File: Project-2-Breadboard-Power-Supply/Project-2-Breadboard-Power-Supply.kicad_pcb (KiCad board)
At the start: 2 copper layers, 35.1 x 53.3 mm, 17 parts, among them J1 Conn_01x02_Pin, J2 Conn_01x02_Pin, J3 Conn_01x03_Pin, J4 Conn_01x03_Pin, J5 Screw_Terminal_01x02, J6 Barrel_Jack_Switch, J7 Screw_Terminal_01x02, U1 LM7805_TO220, U2 LM317_TO-220

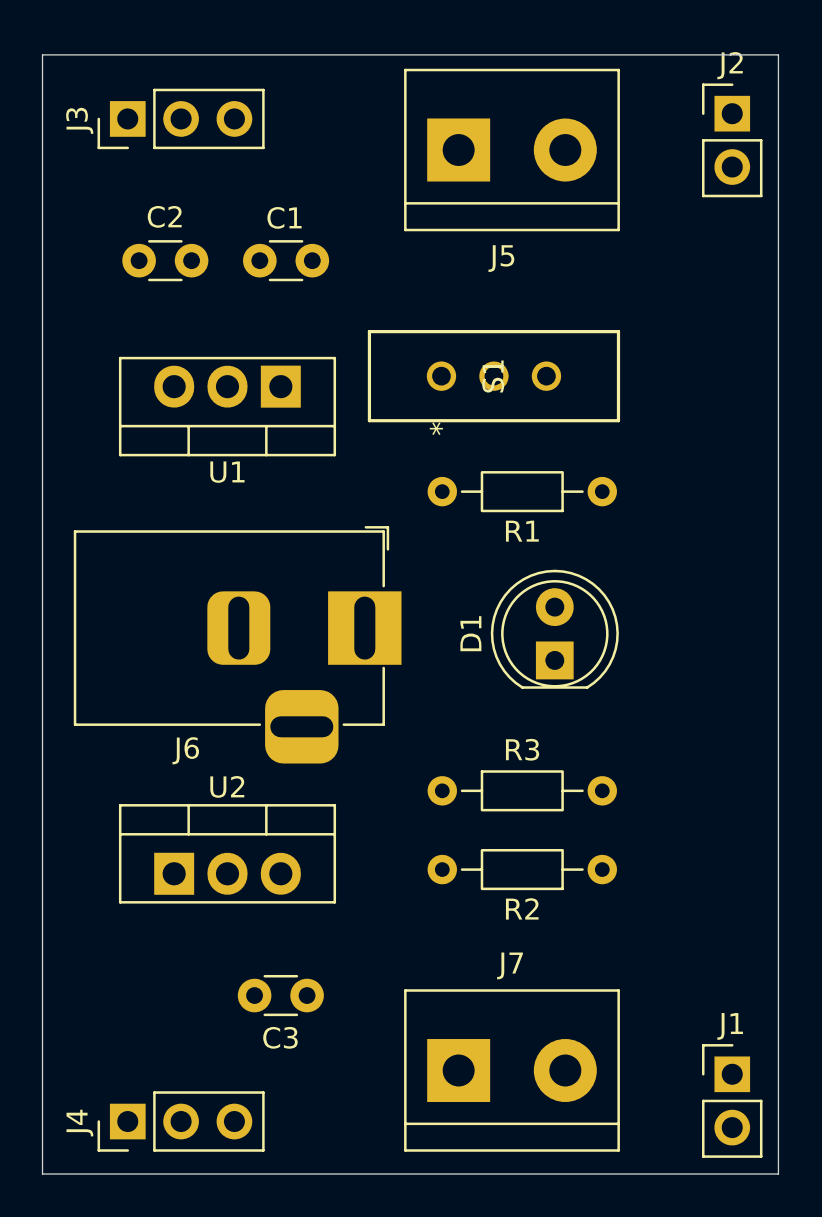
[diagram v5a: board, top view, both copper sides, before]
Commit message: update footprints' placement, and PCB's edge cuts
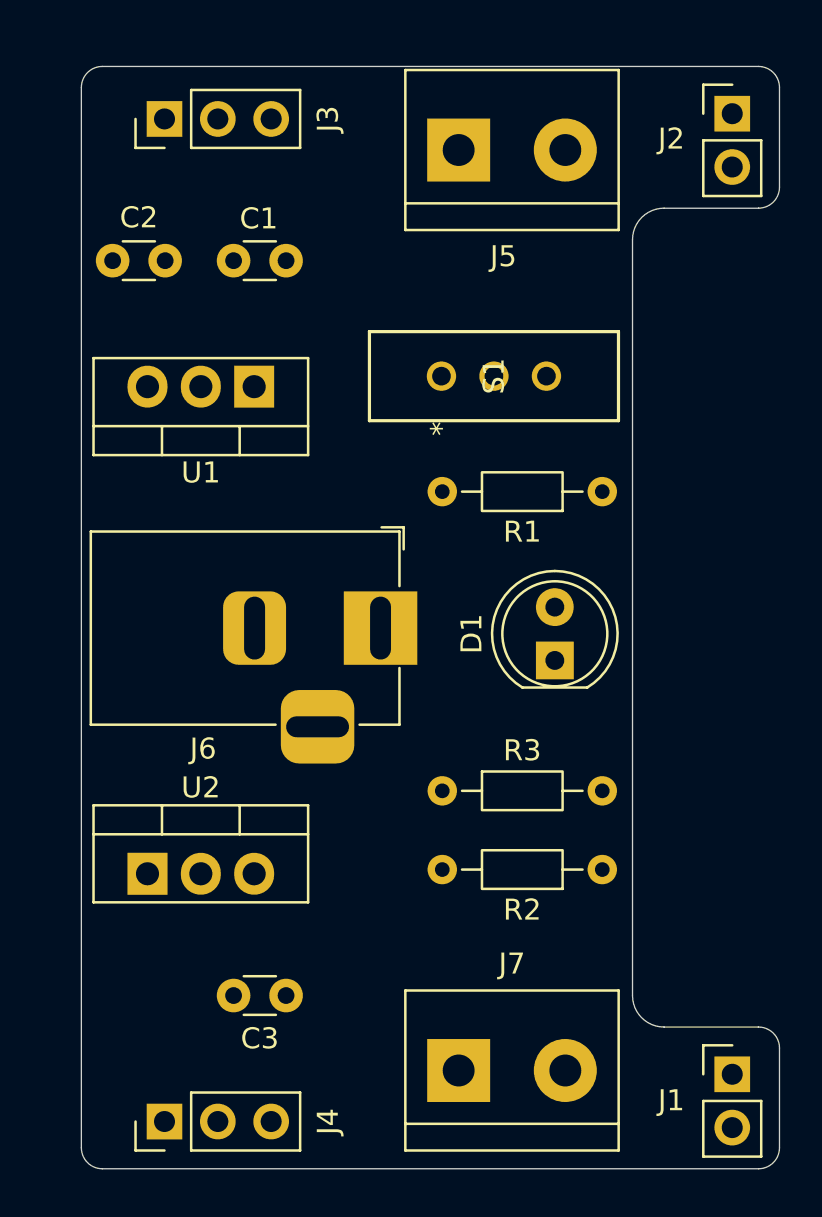
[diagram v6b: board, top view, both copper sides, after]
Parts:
- moved J3 1.75 mm to (34.0, 47.8)
- moved J4 1.75 mm to (34.0, 95.5)
- moved U1 1.27 mm to (38.2, 60.5)
- moved U2 1.27 mm to (33.1, 83.7)
- moved C2 1.26 mm to (31.5, 54.5)
- moved C1 1.25 mm to (39.8, 54.5)
- moved C3 1.00 mm to (39.8, 89.5)
- moved J6 0.75 mm to (44.2, 72.0)
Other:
- board size 35.1 x 53.3 mm -> 33.2 x 52.5 mm
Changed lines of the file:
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@@
 	(footprint "Connector_PinHeader_2.54mm:PinHeader_1x03_P2.54mm_Vertical"
 		(layer "F.Cu")
-		(at 32.21 95.5 90)
+		(at 33.96 95.5 90)
 		(descr "Through hole straight pin header, 1x03, 2.54mm pitch, single row")
 		(tags "Through hole pin header THT 1x03 2.54mm single row")
 		(property "Reference" "J4"
-			(at 0 -2.38 90)
+			(at 0 7.79 90)
 			(layer "F.SilkS")
 			(effects
@@
 	(footprint "Capacitor_THT:C_Disc_D3.0mm_W1.6mm_P2.50mm"
 		(layer "F.Cu")
-		(at 32.75 54.5)
+		(at 31.49 54.5)
 		(descr "C, Disc series, Radial, pin pitch=2.50mm, diameter*width=3.0*1.6mm^2, Capacitor, http://www.vishay.com/docs/45233/krseries.pdf")
 		(tags "C Disc series Radial pin pitch 2.50mm diameter 3.0mm width 1.6mm Capacitor")
@@
 	(footprint "Connector_PinHeader_2.54mm:PinHeader_1x03_P2.54mm_Vertical"
 		(layer "F.Cu")
-		(at 32.21 47.75 90)
+		(at 33.96 47.75 90)
 		(descr "Through hole straight pin header, 1x03, 2.54mm pitch, single row")
 		(tags "Through hole pin header THT 1x03 2.54mm single row")
 		(property "Reference" "J3"
-			(at 0 -2.38 90)
+			(at 0 7.79 90)
 			(layer "F.SilkS")
 			(effects
@@
 		(tags "Through hole pin header THT 1x02 2.54mm single row")
 		(property "Reference" "J2"
-			(at 0 -2.38 0)
+			(at -2.9 1.2 0)
 			(layer "F.SilkS")
 			(effects
@@
 	(footprint "Capacitor_THT:C_Disc_D3.0mm_W1.6mm_P2.50mm"
 		(layer "F.Cu")
-		(at 40.75 89.5 180)
+		(at 39.75 89.5 180)
 		(descr "C, Disc series, Radial, pin pitch=2.50mm, diameter*width=3.0*1.6mm^2, Capacitor, http://www.vishay.com/docs/45233/krseries.pdf")
 		(tags "C Disc series Radial pin pitch 2.50mm diameter 3.0mm width 1.6mm Capacitor")
@@
 	(footprint "Package_TO_SOT_THT:TO-220-3_Vertical"
 		(layer "F.Cu")
-		(at 34.42 83.7)
+		(at 33.15 83.7)
 		(descr "TO-220-3, Vertical, RM 2.54mm, see https://www.vishay.com/docs/66542/to-220-1.pdf")
 		(tags "TO-220-3 Vertical RM 2.54mm")
@@
 		(tags "Through hole pin header THT 1x02 2.54mm single row")
 		(property "Reference" "J1"
-			(at 0 -2.38 0)
+			(at -2.9 1.25 0)
 			(layer "F.SilkS")
 			(effects
@@
 	(footprint "Connector_BarrelJack:BarrelJack_Horizontal"
 		(layer "F.Cu")
-		(at 43.5 72)
+		(at 44.25 72)
 		(descr "DC Barrel Jack")
 		(tags "Power Jack")
@@
 	(footprint "Capacitor_THT:C_Disc_D3.0mm_W1.6mm_P2.50mm"
 		(layer "F.Cu")
-		(at 41 54.5 180)
+		(at 39.75 54.5 180)
 		(descr "C, Disc series, Radial, pin pitch=2.50mm, diameter*width=3.0*1.6mm^2, Capacitor, http://www.vishay.com/docs/45233/krseries.pdf")
 		(tags "C Disc series Radial pin pitch 2.50mm diameter 3.0mm width 1.6mm Capacitor")
@@
 	(footprint "Package_TO_SOT_THT:TO-220-3_Vertical"
 		(layer "F.Cu")
-		(at 39.5 60.5 180)
+		(at 38.23 60.5 180)
 		(descr "TO-220-3, Vertical, RM 2.54mm, see https://www.vishay.com/docs/66542/to-220-1.pdf")
 		(tags "TO-220-3 Vertical RM 2.54mm")
@@
 		)
 	)
-	(gr_rect
-		(start 28.15 44.7)
-		(end 63.2 98)
+	(gr_arc
+		(start 30 46.25)
+		(mid 30.292893 45.542893)
+		(end 31 45.25)
+		(stroke
+			(width 0.05)
+			(type default)
+		)
+		(layer "Edge.Cuts")
+	)
+	(gr_line
+		(start 30 96.75)
+		(end 30 46.25)
+		(stroke
+			(width 0.05)
+			(type default)
+		)
+		(layer "Edge.Cuts")
+	)
+	(gr_arc
+		(start 31 97.75)
+		(mid 30.292893 97.457107)
+		(end 30 96.75)
+		(stroke
+			(width 0.05)
+			(type default)
+		)
+		(layer "Edge.Cuts")
+	)
+	(gr_line
+		(start 56.25 53.5)
+		(end 56.25 89.5)
+		(stroke
+			(width 0.05)
+			(type default)
+		)
+		(layer "Edge.Cuts")
+	)
+	(gr_arc
+		(start 56.25 53.5)
+		(mid 56.68934 52.43934)
+		(end 57.75 52)
+		(stroke
+			(width 0.05)
+			(type default)
+		)
+		(layer "Edge.Cuts")
+	)
+	(gr_arc
+		(start 57.75 91)
+		(mid 56.68934 90.56066)
+		(end 56.25 89.5)
+		(stroke
+			(width 0.05)
+			(type default)
+		)
+		(layer "Edge.Cuts")
+	)
+	(gr_line
+		(start 62.25 45.25)
+		(end 31 45.25)
+		(stroke
+			(width 0.05)
+			(type default)
+		)
+		(layer "Edge.Cuts")
+	)
+	(gr_arc
+		(start 62.25 45.25)
+		(mid 62.957107 45.542893)
+		(end 63.25 46.25)
+		(stroke
+			(width 0.05)
+			(type default)
+		)
+		(layer "Edge.Cuts")
+	)
+	(gr_line
+		(start 62.25 52)
+		(end 57.75 52)
+		(stroke
+			(width 0.05)
+			(type default)
+		)
+		(layer "Edge.Cuts")
+	)
+	(gr_line
+		(start 62.25 91)
+		(end 57.75 91)
+		(stroke
+			(width 0.05)
+			(type default)
+		)
+		(layer "Edge.Cuts")
+	)
+	(gr_arc
+		(start 62.25 91)
+		(mid 62.957107 91.292893)
+		(end 63.25 92)
+		(stroke
+			(width 0.05)
+			(type default)
+		)
+		(layer "Edge.Cuts")
+	)
+	(gr_line
+		(start 62.25 97.75)
+		(end 31 97.75)
+		(stroke
+			(width 0.05)
+			(type default)
+		)
+		(layer "Edge.Cuts")
+	)
+	(gr_line
+		(start 63.25 46.25)
+		(end 63.25 51)
+		(stroke
+			(width 0.05)
+			(type default)
+		)
+		(layer "Edge.Cuts")
+	)
+	(gr_arc
+		(start 63.25 51)
+		(mid 62.957107 51.707107)
+		(end 62.25 52)
+		(stroke
+			(width 0.05)
+			(type default)
+		)
+		(layer "Edge.Cuts")
+	)
+	(gr_arc
+		(start 63.25 96.75)
+		(mid 62.957107 97.457107)
+		(end 62.25 97.75)
+		(stroke
+			(width 0.05)
+			(type default)
+		)
+		(layer "Edge.Cuts")
+	)
+	(gr_line
+		(start 63.25 96.75)
+		(end 63.25 92)
 		(stroke
 			(width 0.05)
 			(type default)
 		)
-		(fill no)
 		(layer "Edge.Cuts")
 	)

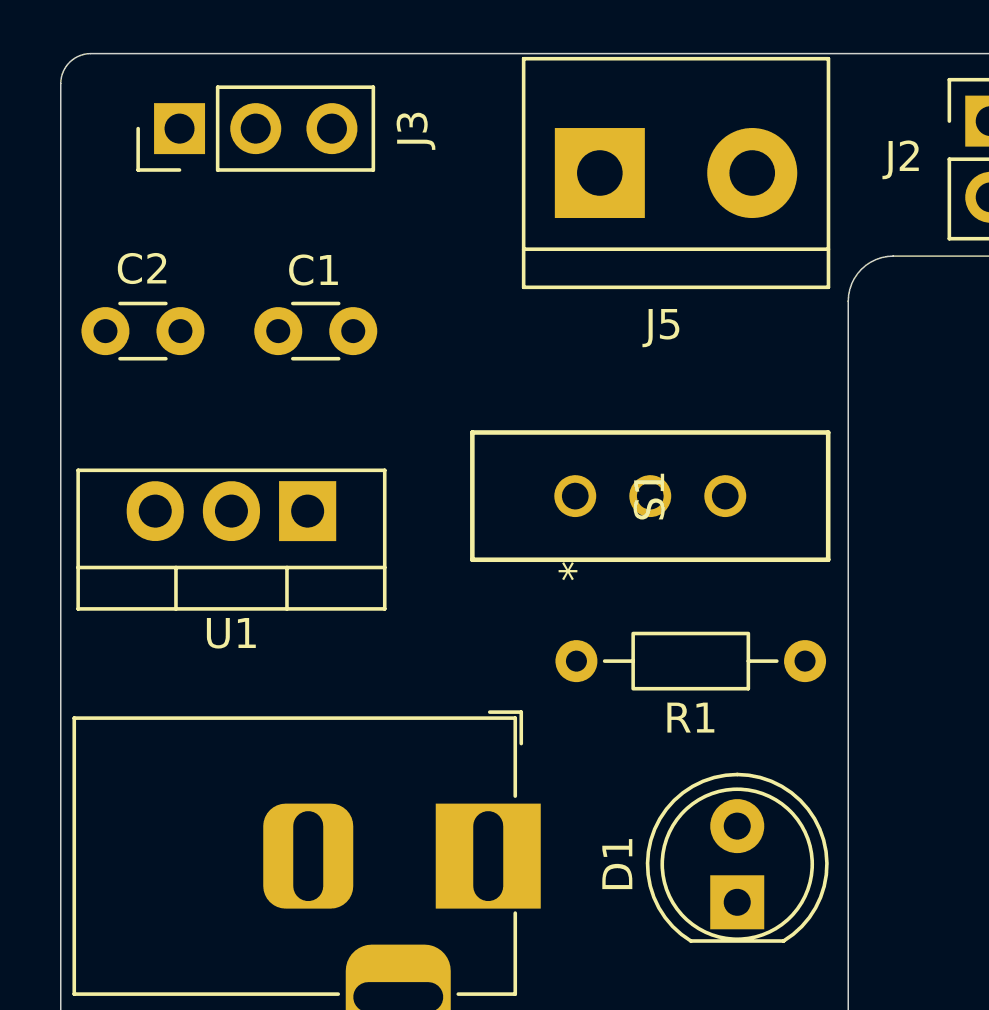
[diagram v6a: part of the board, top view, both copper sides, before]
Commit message: routing started, added via for connecting to pins through the Back copper layer
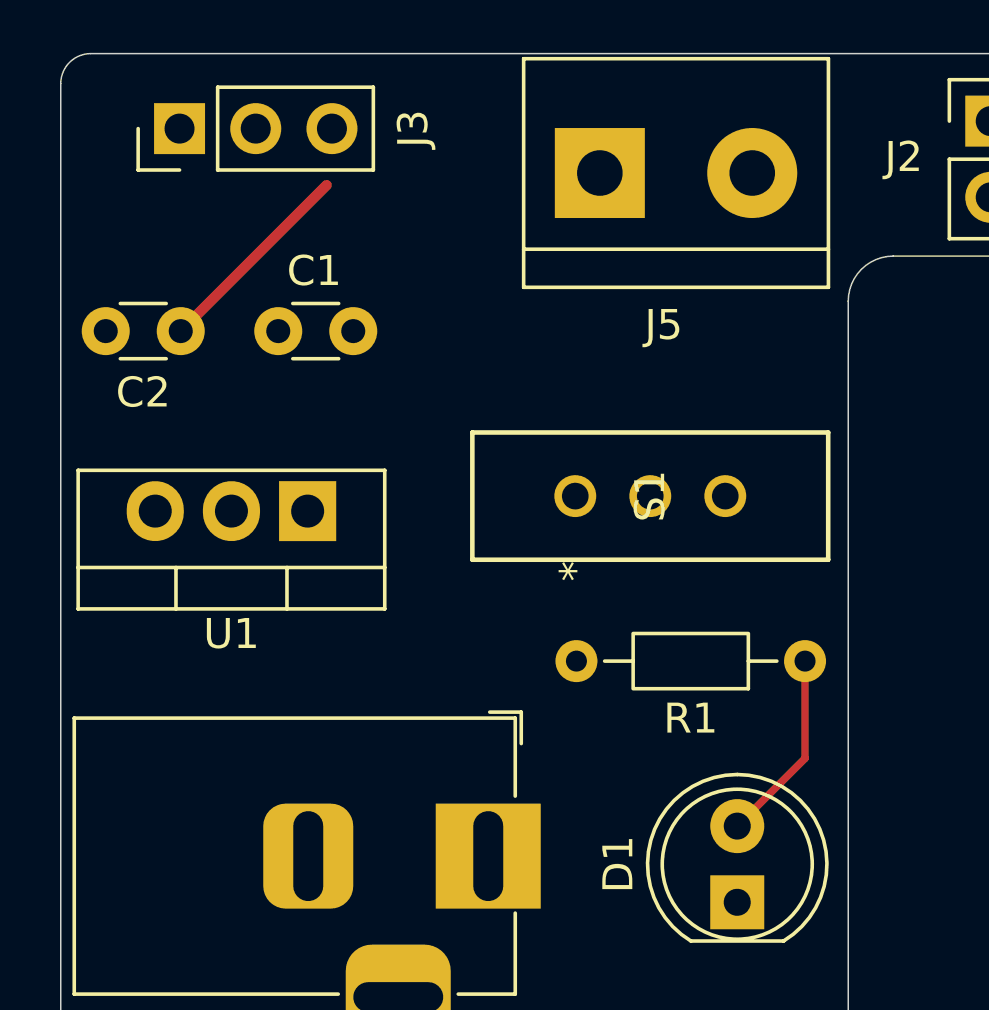
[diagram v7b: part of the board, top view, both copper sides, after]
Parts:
- moved C2 2.51 mm to (34.0, 54.5), turned to 180 degrees
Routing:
- net /5V_net: track 0.00 -> 6.88 mm
- net Net-(D1-A): track 0.00 -> 6.44 mm
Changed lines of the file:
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@@
 		(capping no)
 		(filling no)
+		(zone_defaults)
 		(pcbplotparams
 			(layerselection 0x00000000_00000000_55555555_5755f5ff)
@@
 	(footprint "Capacitor_THT:C_Disc_D3.0mm_W1.6mm_P2.50mm"
 		(layer "F.Cu")
-		(at 31.49 54.5)
+		(at 34 54.5 180)
 		(descr "C, Disc series, Radial, pin pitch=2.50mm, diameter*width=3.0*1.6mm^2, Capacitor, http://www.vishay.com/docs/45233/krseries.pdf")
 		(tags "C Disc series Radial pin pitch 2.50mm diameter 3.0mm width 1.6mm Capacitor")
@@
 		)
 		(property "MPN" ""
-			(at 0 0 0)
+			(at 0 0 180)
 			(unlocked yes)
 			(layer "F.Fab")
@@
 		)
 		(property "Manufacturer" ""
-			(at 0 0 0)
+			(at 0 0 180)
 			(unlocked yes)
 			(layer "F.Fab")
@@
 		(duplicate_pad_numbers_are_jumpers no)
 		(fp_line
-			(start 0.485 -0.92)
-			(end 2.015 -0.92)
+			(start 2.015 0.92)
+			(end 0.485 0.92)
 			(stroke
 				(width 0.12)
@@
 		)
 		(fp_line
-			(start 2.015 0.92)
-			(end 0.485 0.92)
+			(start 0.485 -0.92)
+			(end 2.015 -0.92)
 			(stroke
 				(width 0.12)
@@
 		)
 		(pad "1" thru_hole circle
-			(at 0 0)
+			(at 0 0 180)
 			(size 1.6 1.6)
 			(drill 0.8)
@@
 		)
 		(pad "2" thru_hole circle
-			(at 2.5 0)
+			(at 2.5 0 180)
 			(size 1.6 1.6)
 			(drill 0.8)
@@
 	)
 	(footprint "Resistor_THT:R_Axial_DIN0204_L3.6mm_D1.6mm_P7.62mm_Horizontal"
-		(locked yes)
 		(layer "F.Cu")
 		(at 54.81 65.5 180)
@@
 		(layer "Edge.Cuts")
 	)
+	(segment
+		(start 38.862 49.638)
+		(end 34 54.5)
+		(width 0.35)
+		(layer "F.Cu")
+		(net "/5V_net")
+	)
+	(segment
+		(start 54.81 68.74)
+		(end 52.55 71)
+		(width 0.25)
+		(layer "F.Cu")
+		(net "Net-(D1-A)")
+	)
+	(segment
+		(start 54.81 65.5)
+		(end 54.81 68.74)
+		(width 0.25)
+		(layer "F.Cu")
+		(net "Net-(D1-A)")
+	)
 	(embedded_fonts no)

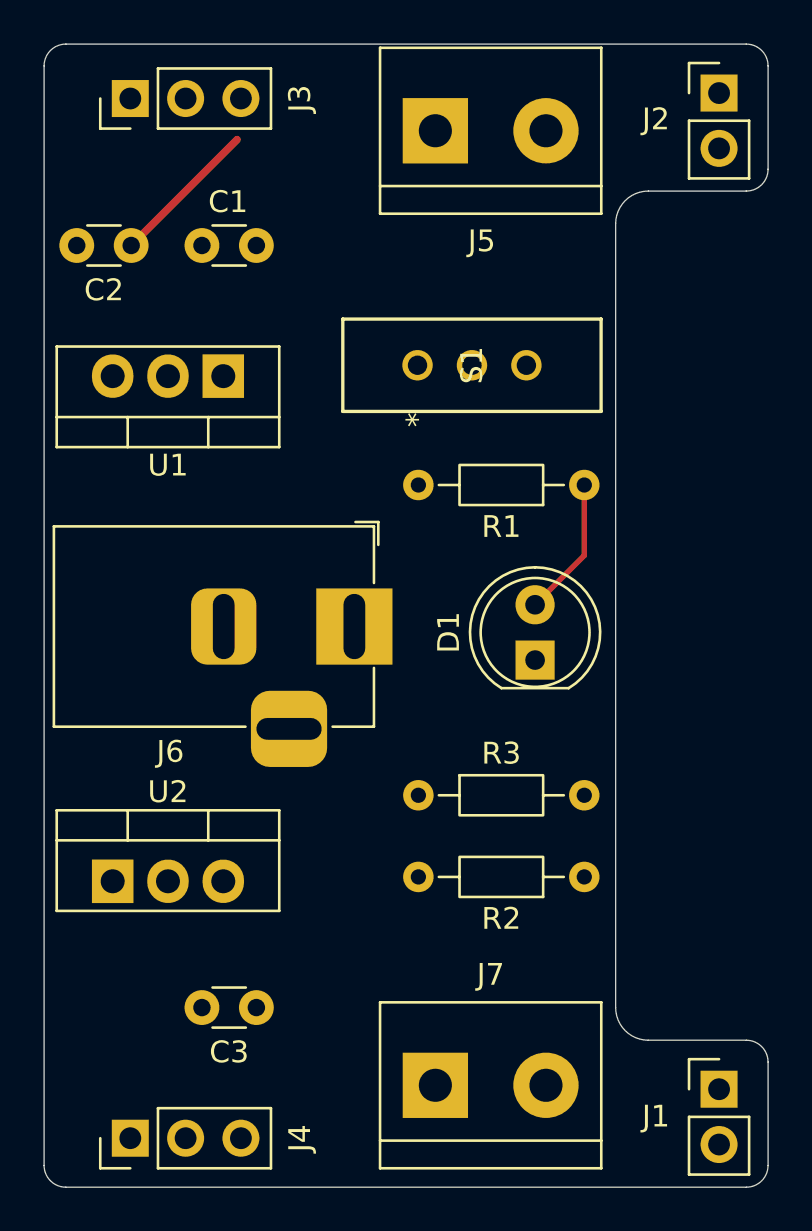
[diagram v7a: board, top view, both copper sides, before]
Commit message: add all routing but GND
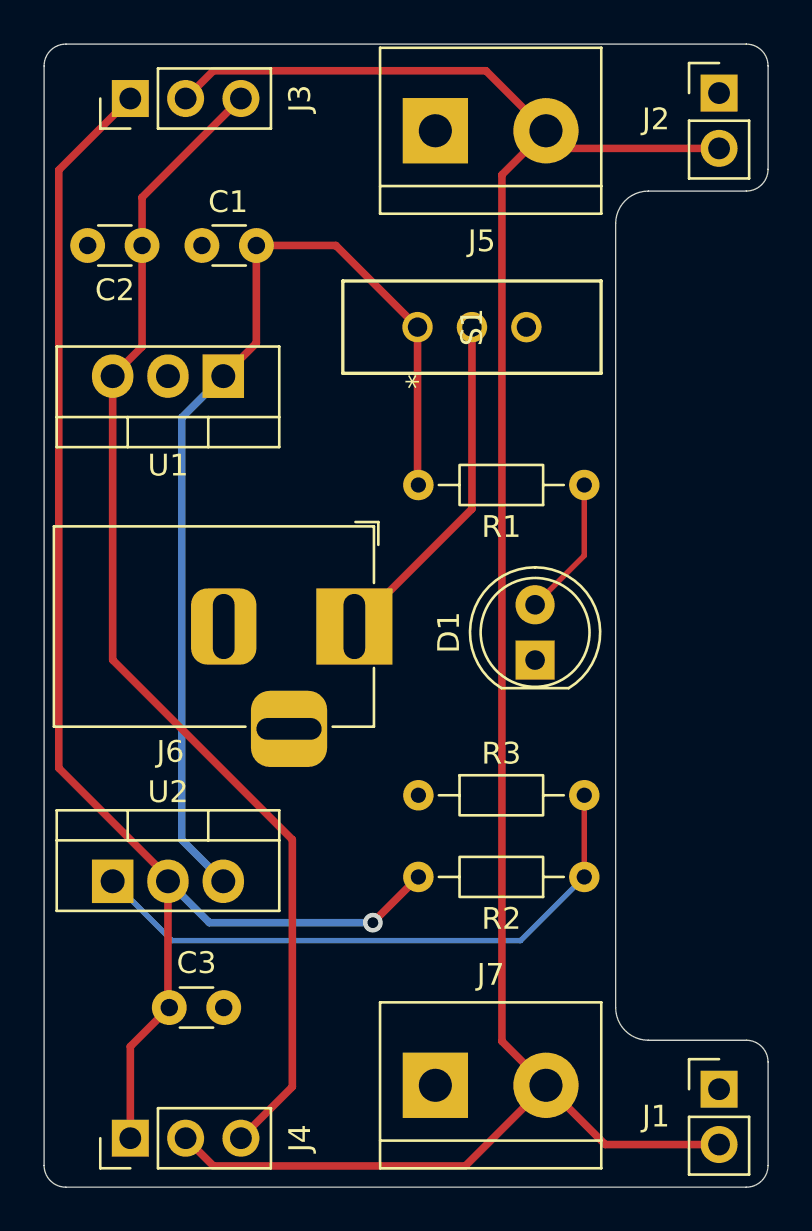
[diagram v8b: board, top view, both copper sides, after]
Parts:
- moved C3 4.00 mm to (35.8, 89.5), turned to 0 degrees
- moved S1 1.75 mm to (47.2, 58.2)
- moved C2 0.50 mm to (34.5, 54.5)
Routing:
- net /PWR_output: track 0.00 -> 99.9 mm
- net /3v3_net: track 0.00 -> 65.4 mm, vias 0 -> 1
- net /5V_net: track 6.88 -> 54.6 mm
- net /12V_net: track 0.00 -> 47.6 mm
- net Net-(U2-ADJ): track 0.00 -> 27.8 mm
- net /PWR_input: track 0.00 -> 16.0 mm
